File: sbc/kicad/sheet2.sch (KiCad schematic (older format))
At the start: 6 parts, among them U18 62256 RAM, U19 27128, U20 MC6802, Y2 3.579545 kHz

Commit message: Updates, start of PCB.
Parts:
- C24, C25: footprint (none) -> Capacitor_THT:C_Disc_D5.0mm_W2.5mm_P5.00mm
- Y2: footprint (none) -> Crystal:Crystal_HC18-U_Vertical
- renumbered U18 to U19, U19 to U20, U20 to U21
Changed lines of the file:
@@
 Sheet 5 6
 Title "6800 SIngle Board Computer"
-Date "2022-01-14"
+Date "2022-01-22"
 Rev "0.1"
 Comp "Jeff Tranter"
@@
 F 0 "C25" H 2115 5096 50  0000 L CNN
 F 1 "30 pF" H 2115 5005 50  0000 L CNN
-F 2 "" H 2038 4900 50  0001 C CNN
+F 2 "Capacitor_THT:C_Disc_D5.0mm_W2.5mm_P5.00mm" H 2038 4900 50  0001 C CNN
 F 3 "~" H 2000 5050 50  0001 C CNN
 	1    2000 5050
@@
 $EndComp
 $Comp
-L Memory_EPROM:27128 U19
+L Memory_EPROM:27128 U20
 U 1 1 61DA2B2B
 P 9200 3350
-F 0 "U19" H 9200 3350 50  0000 C CNN
+F 0 "U20" H 9200 3350 50  0000 C CNN
 F 1 "27128" H 9250 3250 50  0000 C CNN
 F 2 "Package_DIP:DIP-28_W15.24mm" H 9200 3350 50  0001 C CNN
@@
 F 0 "C24" H 1586 5004 50  0000 R CNN
 F 1 "30 pF" H 1586 5095 50  0000 R CNN
-F 2 "" H 1738 4900 50  0001 C CNN
+F 2 "Capacitor_THT:C_Disc_D5.0mm_W2.5mm_P5.00mm" H 1738 4900 50  0001 C CNN
 F 3 "~" H 1700 5050 50  0001 C CNN
 	1    1700 5050
@@
 F 0 "Y2" H 1400 4800 50  0000 C CNN
 F 1 "3.579545 kHz" H 1400 4700 50  0000 C CNN
-F 2 "" H 1850 4750 50  0001 C CNN
+F 2 "Crystal:Crystal_HC18-U_Vertical" H 1850 4750 50  0001 C CNN
 F 3 "~" H 1850 4750 50  0001 C CNN
 	1    1850 4750
@@
 D6
 $Comp
-L CPU_NXP_6800:MC6802 U20
+L CPU_NXP_6800:MC6802 U21
 U 1 1 61EF4887
 P 2850 3650
-F 0 "U20" H 2850 4150 50  0000 C CNN
+F 0 "U21" H 2850 4150 50  0000 C CNN
 F 1 "MC6802" H 2850 4000 50  0000 C CNN
 F 2 "Package_DIP:DIP-40_W15.24mm" H 2850 2150 50  0001 C CNN
@@
 	2250 3850 2350 3850
 $Comp
-L power:VCC #PWR050
+L power:VCC #PWR051
 U 1 1 61DEF516
 P 2950 2250
-F 0 "#PWR050" H 2950 2100 50  0001 C CNN
+F 0 "#PWR051" H 2950 2100 50  0001 C CNN
 F 1 "VCC" H 2967 2423 50  0000 C CNN
 F 2 "" H 2950 2250 50  0001 C CNN
@@
 	8600 4250 8800 4250
 $Comp
-L Memory_RAM:CY62256-70PC U18
+L Memory_RAM:CY62256-70PC U19
 U 1 1 61DA8011
 P 6000 3200
-F 0 "U18" H 6000 3600 50  0000 C CNN
+F 0 "U19" H 6000 3600 50  0000 C CNN
 F 1 "62256 RAM" H 6000 3450 50  0000 C CNN
 F 2 "Package_DIP:DIP-28_W15.24mm" H 6000 3100 50  0001 C CNN
@@
 $EndComp
 $Comp
-L power:VCC #PWR049
+L power:VCC #PWR050
 U 1 1 61E46926
 P 6000 2200
-F 0 "#PWR049" H 6000 2050 50  0001 C CNN
+F 0 "#PWR050" H 6000 2050 50  0001 C CNN
 F 1 "VCC" H 6017 2373 50  0000 C CNN
 F 2 "" H 6000 2200 50  0001 C CNN
@@
 	9200 4550 9200 4450
 $Comp
-L power:VCC #PWR048
+L power:VCC #PWR049
 U 1 1 61EA8E72
 P 9200 2150
-F 0 "#PWR048" H 9200 2000 50  0001 C CNN
+F 0 "#PWR049" H 9200 2000 50  0001 C CNN
 F 1 "VCC" H 9217 2323 50  0000 C CNN
 F 2 "" H 9200 2150 50  0001 C CNN
@@
 ROM (16K)
 $Comp
-L power:GND #PWR0105
+L power:GND #PWR052
 U 1 1 61F45D94
 P 2350 3450
-F 0 "#PWR0105" H 2350 3200 50  0001 C CNN
+F 0 "#PWR052" H 2350 3200 50  0001 C CNN
 F 1 "GND" V 2355 3322 50  0000 R CNN
 F 2 "" H 2350 3450 50  0001 C CNN

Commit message: Some fixes based on prototyping work.
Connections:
- net A6: now also U19.4 (A6)
- net A7: no longer U19.4 (A6)
- net VCC: now also U20.1 (VPP)
- no-connect marks 1 -> 0
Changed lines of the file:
@@
 Sheet 5 6
 Title "6800 SIngle Board Computer"
-Date "2022-01-22"
+Date "2022-02-06"
 Rev "0.1"
 Comp "Jeff Tranter"
@@
 $EndComp
 Wire Wire Line
-	8600 3950 8800 3950
-NoConn ~ 8800 4050
+	8600 3950 8700 3950
 Text GLabel 8600 4150 0    50   Input ~ 0
 ~ROMEN
@@
 A5
 Text GLabel 5300 3100 0    50   Input ~ 0
-A7
+A6
 Text GLabel 5300 3200 0    50   Input ~ 0
 A7
@@
 	0    1    1    0
 $EndComp
+Wire Wire Line
+	8800 4050 8700 4050
+Wire Wire Line
+	8700 4050 8700 3950
+Connection ~ 8700 3950
+Wire Wire Line
+	8700 3950 8800 3950
 $EndSCHEMATC

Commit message: Getting close to ready to order PCBs. Check in all files.
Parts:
- U19: value 62256 RAM -> 62256
- Y2: value 3.579545 kHz -> 3.579545 MHz
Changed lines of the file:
@@
 Sheet 5 6
 Title "6800 SIngle Board Computer"
-Date "2022-02-09"
+Date "2022-02-12"
 Rev "0.1"
 Comp "Jeff Tranter"
@@
 P 1850 4750
 F 0 "Y2" H 1400 4800 50  0000 C CNN
-F 1 "3.579545 kHz" H 1400 4700 50  0000 C CNN
+F 1 "3.579545 MHz" H 1400 4700 50  0000 C CNN
 F 2 "Crystal:Crystal_HC18-U_Vertical" H 1850 4750 50  0001 C CNN
 F 3 "~" H 1850 4750 50  0001 C CNN
@@
 P 6000 3200
 F 0 "U19" H 6000 3600 50  0000 C CNN
-F 1 "62256 RAM" H 6000 3450 50  0000 C CNN
+F 1 "62256" H 6000 3450 50  0000 C CNN
 F 2 "Package_DIP:DIP-28_W15.24mm" H 6000 3100 50  0001 C CNN
 F 3 "https://ecee.colorado.edu/~mcclurel/Cypress_SRAM_CY62256.pdf" H 6000 3100 50  0001 C CNN

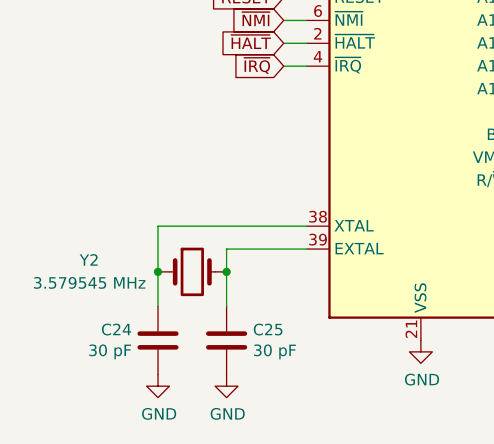
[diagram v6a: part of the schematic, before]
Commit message: Some corrections to schematic and added to documentation.
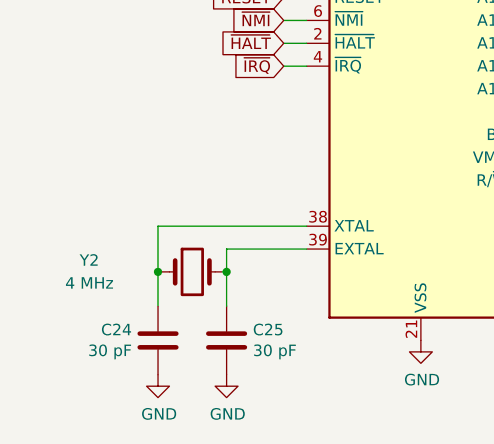
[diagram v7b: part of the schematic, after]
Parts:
- Y2: value 3.579545 MHz -> 4 MHz
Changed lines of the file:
@@
 Sheet 5 6
 Title "6800 SIngle Board Computer"
-Date "2022-02-12"
-Rev "0.1"
+Date "2022-03-02"
+Rev "1.0"
 Comp "Jeff Tranter"
 Comment1 ""
@@
 P 1850 4750
 F 0 "Y2" H 1400 4800 50  0000 C CNN
-F 1 "3.579545 MHz" H 1400 4700 50  0000 C CNN
+F 1 "4 MHz" H 1400 4700 50  0000 C CNN
 F 2 "Crystal:Crystal_HC18-U_Vertical" H 1850 4750 50  0001 C CNN
 F 3 "~" H 1850 4750 50  0001 C CNN
